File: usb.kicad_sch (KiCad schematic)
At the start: 26 parts, among them J1 USB_A, J2 USB_A, J4 USB_C_Receptacle_USB2.0, U1 FE1.1s, U3 SRV05-4, U4 SRV05-4, U6 AP2552W6, Y1 12MHz

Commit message: routing progress
Just nice to make some save points every now and again.
USB seems... ok?  Still need to check 3v3 or 5v on the power pullups,
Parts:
- removed U3: SRV05-4, Package_TO_SOT_SMD:SOT-23-6, symbol Power_Protection:SRV05-4
- added U3: SRV05-4, Package_TO_SOT_SMD:SOT-23-6, symbol karl-parts:SRV05-4
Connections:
- net GND: now also U3.2 (GND)
- net UDS1N: now also U1.10 (DM1), U3.6 (I/O4); no longer U1.8 (DM2)
- net UDS1P: now also U1.11 (DP1), U3.1 (I/O1); no longer U1.9 (DP2)
- net UDS2N: now also U1.8 (DM2), U3.4 (I/O3); no longer U1.6 (DM3)
- net UDS2P: now also U1.9 (DP2), U3.3 (I/O2); no longer U1.7 (DP3)
- net UMCU_N: now also U1.6 (DM3); no longer U1.10 (DM1)
- net UMCU_P: now also U1.7 (DP3); no longer U1.11 (DP1)
- net UUPN: now also U4.3 (IO2); no longer U4.1 (IO1)
- net UUPP: now also U4.4 (IO3); no longer U4.3 (IO2)
- net VBUS: now also U3.5 (VBUS)
- no-connect marks 9 -> 11
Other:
- note added: "Do these need to be 3v3?! these are from the switch?"
- note added: "TODO - ground?"
- moved on the sheet: U4

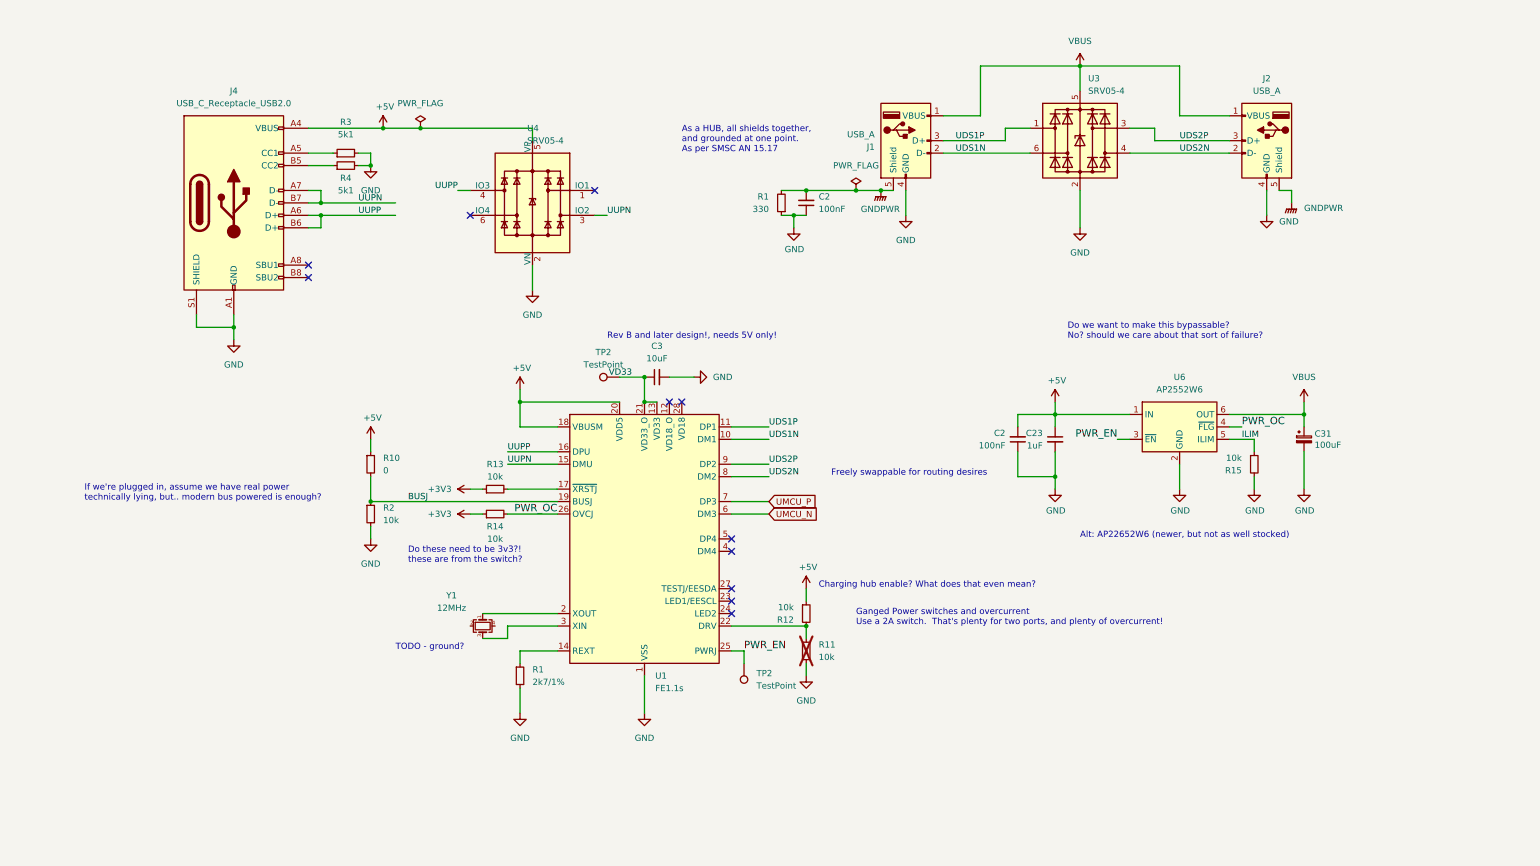
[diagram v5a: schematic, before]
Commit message: cleanup schematic, break out most of it
Broke it all out to the right places, now I can go and shuffle all the
labels to make it line up.  Thankfully we can just "freely" route the
keybaord matrix pins!
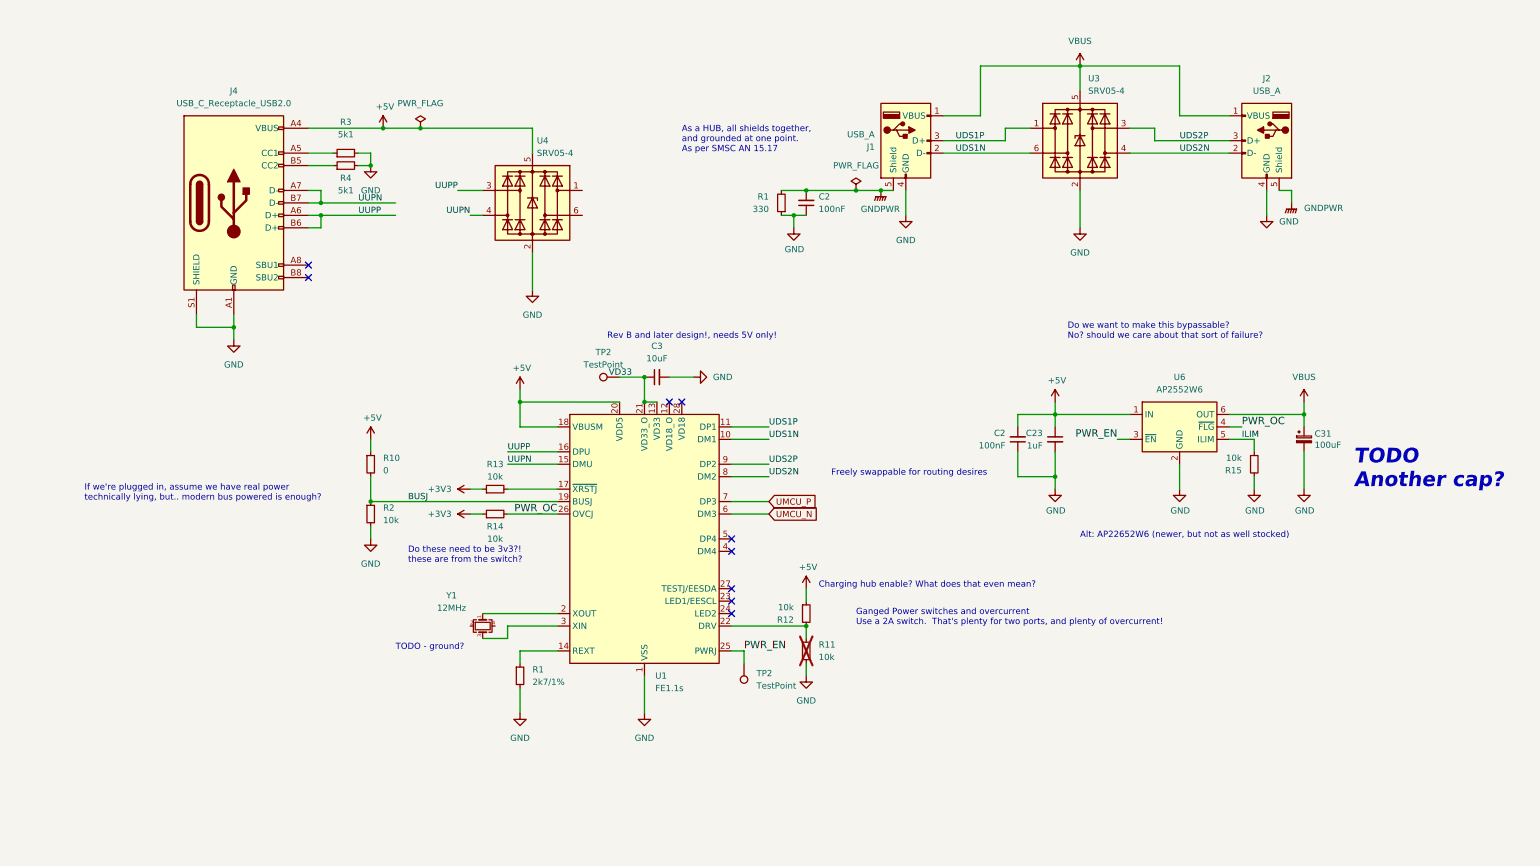
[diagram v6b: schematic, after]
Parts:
- U4: symbol Power_Protection:SRV05-4 -> karl-parts:SRV05-4
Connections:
- net UUPN: now also U4.4 (I/O3); no longer U4.3 (IO2)
- net UUPP: now also U4.3 (I/O2); no longer U4.4 (IO3)
- no-connect marks 11 -> 9
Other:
- note added: "TODO Another cap?"
- company: (none) -> Ekta Labs
- title: (none) -> Das KB4-Bara2
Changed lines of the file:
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@@
 (kicad_sch (version 20230121) (generator eeschema)
   (paper "A4")
+  (title_block
+    (title "Das KB4-Bara2")
+    (company "Ekta Labs")
+    (comment 1 "http://github.com/karlp/das-kb4-bara2")
+  )
   (junction (at 86.36 45.72) (diameter 0) (color 0 0 0 0)
   )
@@
   (no_connect (at 160.02 121.92))
   (no_connect (at 147.32 93.98))
-  (no_connect (at 132.08 50.8))
   (no_connect (at 160.02 124.46))
   (no_connect (at 160.02 137.16))
   (no_connect (at 73.66 68.58))
-  (no_connect (at 106.68 55.88))
   (no_connect (at 160.02 132.08))
   (no_connect (at 149.86 93.98))
@@
     (stroke (width 0) (type default))
   )
+  (wire (pts (xy 106.68 55.88) (xy 109.22 55.88))
+    (stroke (width 0) (type default))
+  )
   (wire (pts (xy 86.36 114.3) (xy 124.46 114.3))
     (stroke (width 0) (type default))
@@
     (stroke (width 0) (type default))
   )
-  (wire (pts (xy 132.08 55.88) (xy 134.62 55.88))
-    (stroke (width 0) (type default))
-  )
   (wire (pts (xy 114.3 139.7) (xy 114.3 142.24))
     (stroke (width 0) (type default))
@@
     (stroke (width 0) (type default))
   )
-  (wire (pts (xy 119.38 66.04) (xy 119.38 71.12))
+  (wire (pts (xy 119.38 63.5) (xy 119.38 71.12))
     (stroke (width 0) (type default))
   )
@@
     (stroke (width 0) (type default))
   )
-  (wire (pts (xy 119.38 40.64) (xy 119.38 38.1))
-    (stroke (width 0) (type default))
-  )
   (wire (pts (xy 218.44 109.22) (xy 226.06 109.22))
     (stroke (width 0) (type default))
@@
     (stroke (width 0) (type default))
   )
+  (wire (pts (xy 119.38 38.1) (xy 119.38 43.18))
+    (stroke (width 0) (type default))
+  )
   (wire (pts (xy 114.3 106.68) (xy 124.46 106.68))
     (stroke (width 0) (type default))
@@
     (stroke (width 0) (type default))
   )
-  (wire (pts (xy 104.14 50.8) (xy 106.68 50.8))
+  (wire (pts (xy 104.14 50.8) (xy 109.22 50.8))
     (stroke (width 0) (type default))
   )
@@
     (effects (font (size 1.27 1.27)) (justify left bottom))
   )
+  (text "TODO\nAnother cap?" (at 287.02 111.76 0)
+    (effects (font (size 3 3) (thickness 0.6) bold italic (color 255 16 105 1)) (justify left bottom))
+  )
   (text "Rev B and later design!, needs 5V only!" (at 134.62 81.28 0)
     (effects (font (size 1.27 1.27)) (justify left bottom))
@@
     (effects (font (size 1.27 1.27)) (justify left bottom))
   )
-  (label "UUPN" (at 134.62 55.88 0) (fields_autoplaced)
-    (effects (font (size 1.27 1.27)) (justify left bottom))
-  )
   (label "UUPN" (at 83.82 53.34 0) (fields_autoplaced)
     (effects (font (size 1.27 1.27)) (justify left bottom))
@@
   (label "UDS2N" (at 251.46 43.18 0) (fields_autoplaced)
     (effects (font (size 1.27 1.27)) (justify left bottom))
+  )
+  (label "UUPN" (at 106.68 55.88 180) (fields_autoplaced)
+    (effects (font (size 1.27 1.27)) (justify right bottom))
   )
   (label "UDS1N" (at 205.74 43.18 0) (fields_autoplaced)
@@
     )
   )
-  (symbol (lib_id "Power_Protection:SRV05-4") (at 119.38 53.34 0) (mirror y) (unit 1)
+  (symbol (lib_id "karl-parts:SRV05-4") (at 119.38 53.34 0) (mirror y) (unit 1)
     (in_bom yes) (on_board yes) (dnp no) (fields_autoplaced)
-    (property "Reference" "U4" (at 118.2939 38.1 0)
+    (property "Reference" "U4" (at 120.2689 40.64 0)
       (effects (font (size 1.27 1.27)) (justify right))
     )
-    (property "Value" "SRV05-4" (at 118.2939 40.64 0)
+    (property "Value" "SRV05-4" (at 120.2689 43.18 0)
       (effects (font (size 1.27 1.27)) (justify right))
     )
-    (property "Footprint" "Package_TO_SOT_SMD:SOT-23-6" (at 101.6 64.77 0)
-      (effects (font (size 1.27 1.27)) hide)
-    )
-    (property "Datasheet" "http://www.onsemi.com/pub/Collateral/SRV05-4-D.PDF" (at 119.38 53.34 0)
-      (effects (font (size 1.27 1.27)) hide)
-    )
+    (property "Footprint" "Package_TO_SOT_SMD:SOT-23-6" (at 119.38 66.04 0)
+      (effects (font (size 1.27 1.27)) hide)
+    )
+    (property "Datasheet" "http://www.onsemi.com/pub/Collateral/SRV05-4-D.PDF" (at 114.3 44.45 0)
+      (effects (font (size 1.27 1.27)) hide)
+    )

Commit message: unrouted: 0
Juggled all the key matrix IOs and reviewed "all" outstanding TODOs

left: add another cap for downstream Vbus.  it's free, and can only
help.

left: lots of silk?
left: place as much free io to pads as can be easily done, for
test/board reuse.
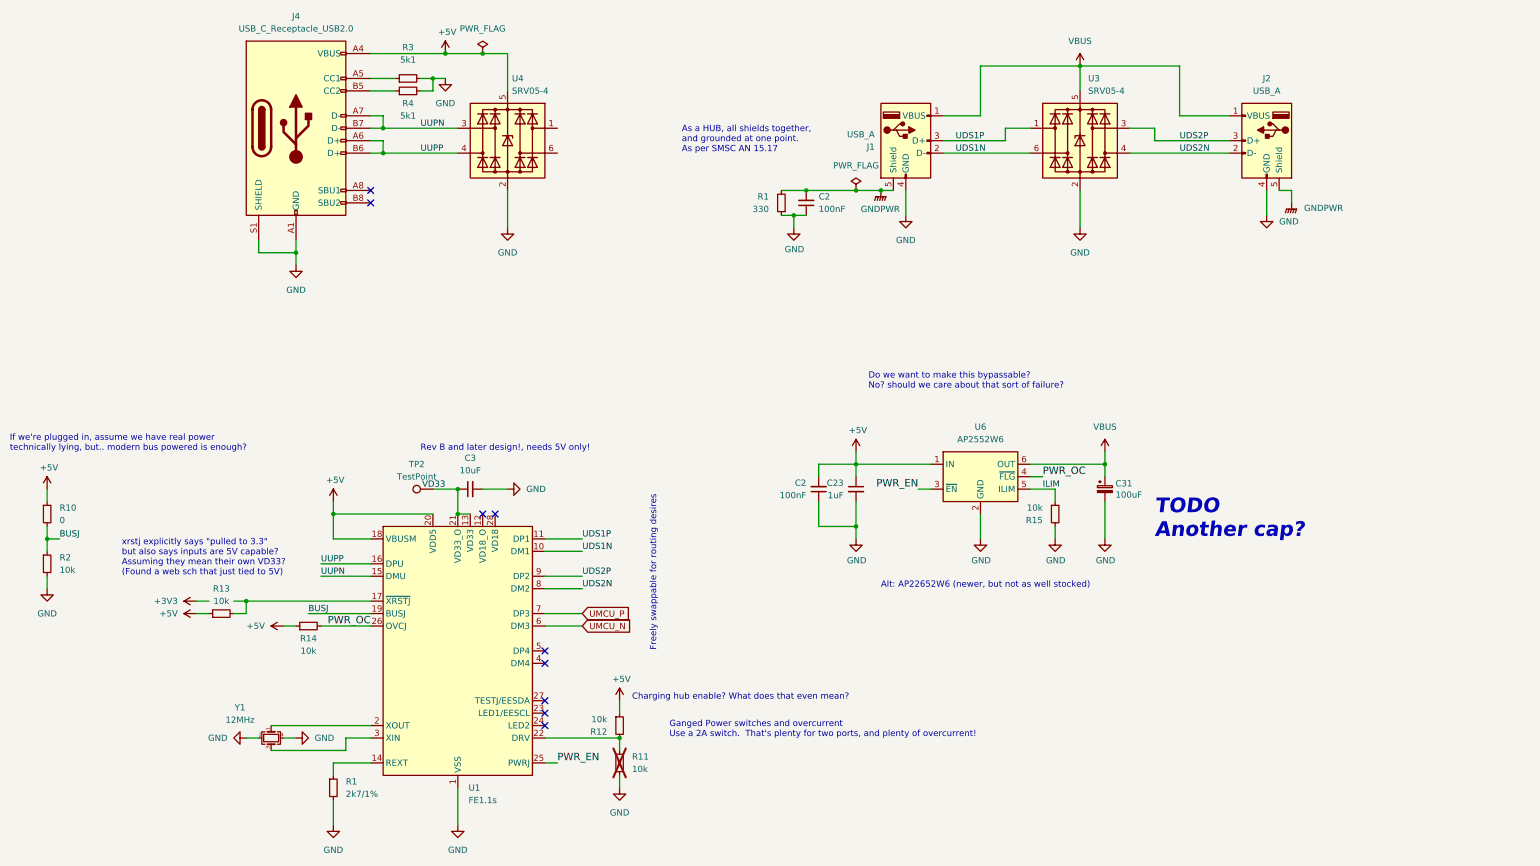
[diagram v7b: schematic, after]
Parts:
- removed TP2: TestPoint, TestPoint:TestPoint_THTPad_D1.5mm_Drill0.7mm, symbol Connector:TestPoint
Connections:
- net +3V3: no longer R13.1, R14.1
- net +5V: now also R13.1, R14.1
- net GND: now also Y1.2, Y1.4
- net UUPN: now also U4.3 (I/O2); no longer U4.4 (I/O3)
- net UUPP: now also U4.4 (I/O3); no longer U4.3 (I/O2)
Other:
- note added: "xrstj explicitly says "pulled to 3.3" but also says inputs are 5V capable? Assuming they mean their own VD33? (Found a web sch that just tied to 5V)"
- note removed: "Do these need to be 3v3?! these are from the switch?"
- note removed: "TODO - ground?"
- moved on the sheet: C2, C23, C3, C31, J4, R1, R10, R11, R12, R13, R14, R15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

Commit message: shuffled, added bonus, silked up...
Nearly there..?
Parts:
- added C31: 100uF, Capacitor_SMD:C_1206_3216Metric, symbol Device:C_Polarized_Small
- R1: value 330 -> 220; MPN 0603WAF3300T5E -> 0603WAF2200T5E; lcsc# C23138 -> C22962
- TP2: value TestPoint -> VD33
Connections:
- net GND: now also C31.2
- net VBUS: now also C31.1
- no-connect marks 9 -> 11
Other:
- note added: "Charging hub enable? What does that even mean? (allegedly, means can give dumb DS devs >= 500mA?)"
- note removed: "Charging hub enable? What does that even mean?"
- note removed: "Do we want to make this bypassable? No? should we care about that sort of failure?"
- note removed: "TODO Another cap?"
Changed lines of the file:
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@@
   (junction (at 172.72 55.88) (diameter 0) (color 0 0 0 0)
+  )
+  (junction (at 236.22 119.38) (diameter 0) (color 0 0 0 0)
   )
   (junction (at 104.14 111.76) (diameter 0) (color 0 0 0 0)
@@
   (no_connect (at 121.92 147.32))
   (no_connect (at 121.92 160.02))
+  (no_connect (at 124.46 43.18))
   (no_connect (at 86.36 53.34))
+  (no_connect (at 124.46 38.1))
   (no_connect (at 121.92 154.94))
   (no_connect (at 111.76 116.84))
@@
     (stroke (width 0) (type default))
   )
+  (wire (pts (xy 246.38 106.68) (xy 236.22 106.68))
+    (stroke (width 0) (type default))
+  )
   (wire (pts (xy 121.92 139.7) (xy 129.54 139.7))
     (stroke (width 0) (type default))
@@
     (stroke (width 0) (type default))
   )
+  (wire (pts (xy 246.38 109.22) (xy 246.38 106.68))
+    (stroke (width 0) (type default))
+  )
   (wire (pts (xy 78.74 114.3) (xy 78.74 116.84))
     (stroke (width 0) (type default))
@@
     (stroke (width 0) (type default))
   )
+  (wire (pts (xy 246.38 119.38) (xy 236.22 119.38))
+    (stroke (width 0) (type default))
+  )
   (wire (pts (xy 190.5 50.8) (xy 193.04 50.8))
     (stroke (width 0) (type solid))
@@
     (stroke (width 0) (type default))
   )
-  (wire (pts (xy 236.22 114.3) (xy 236.22 121.92))
+  (wire (pts (xy 236.22 114.3) (xy 236.22 119.38))
     (stroke (width 0) (type solid))
   )
@@
     (stroke (width 0) (type default))
   )
+  (wire (pts (xy 246.38 114.3) (xy 246.38 119.38))
+    (stroke (width 0) (type default))
+  )
   (wire (pts (xy 63.5 63.5) (xy 71.12 63.5))
     (stroke (width 0) (type default))
@@
     (stroke (width 0) (type default))
   )
+  (wire (pts (xy 236.22 119.38) (xy 236.22 121.92))
+    (stroke (width 0) (type solid))
+  )
   (wire (pts (xy 99.06 27.94) (xy 96.52 27.94))
     (stroke (width 0) (type default))
@@
     (effects (font (size 1.27 1.27)) (justify left bottom))
   )
-  (text "Do we want to make this bypassable?\nNo? should we care about that sort of failure?"
-    (at 187.96 91.44 0)
-    (effects (font (size 1.27 1.27)) (justify left bottom))
-  )
   (text "If we're plugged in, assume we have real power\ntechnically lying, but.. modern bus powered is enough?"
     (at 12.7 104.14 0)
     (effects (font (size 1.27 1.27)) (justify left bottom))
   )
-  (text "TODO\nAnother cap?" (at 246.38 121.92 0)
-    (effects (font (size 3 3) (thickness 0.6) bold italic (color 255 16 105 1)) (justify left bottom))
-  )
   (text "Rev B and later design!, needs 5V only!" (at 96.52 104.14 0)
     (effects (font (size 1.27 1.27)) (justify left bottom))
   )
-  (text "Charging hub enable? What does that even mean?" (at 139.7 154.94 0)
+  (text "Charging hub enable? What does that even mean?\n(allegedly, means can give dumb DS devs >= 500mA?)"
+    (at 139.7 154.94 0)
     (effects (font (size 1.27 1.27)) (justify left bottom))
   )
@@
       (effects (font (size 1.27 1.27)) (justify left))
     )
-    (property "Value" "330" (at 167.64 54.61 0)
+    (property "Value" "220" (at 167.64 54.61 0)
       (effects (font (size 1.27 1.27)) (justify left))
     )
@@
       (effects (font (size 1.27 1.27)) hide)
     )
-    (property "MPN" "0603WAF3300T5E" (at 170.18 53.34 0)
+    (property "MPN" "0603WAF2200T5E" (at 170.18 53.34 0)
       (effects (font (size 1.27 1.27)) hide)
     )
@@
       (effects (font (size 1.27 1.27)) hide)
     )
-    (property "lcsc#" "C23138" (at 170.18 53.34 0)
+    (property "lcsc#" "C22962" (at 170.18 53.34 0)
       (effects (font (size 1.27 1.27)) hide)
     )
@@
       (effects (font (size 1.27 1.27)))
     )
-    (property "Value" "TestPoint" (at 95.758 109.22 90)
+    (property "Value" "VD33" (at 95.758 109.22 90)
       (effects (font (size 1.27 1.27)))
     )
@@
         )
       )
+    )
+  )
+  (symbol (lib_id "Device:C_Polarized_Small") (at 246.38 111.76 0) (unit 1)
+    (in_bom yes) (on_board yes) (dnp no)
+    (property "Reference" "C31" (at 248.5391 110.6106 0)
+      (effects (font (size 1.27 1.27)) (justify left))
+    )
+    (property "Value" "100uF" (at 248.539 112.909 0)
+      (effects (font (size 1.27 1.27)) (justify left))
+    )
+    (property "Footprint" "Capacitor_SMD:C_1206_3216Metric" (at 246.38 111.76 0)
+      (effects (font (size 1.27 1.27)) hide)
+    )
+    (property "Datasheet" "~" (at 246.38 111.76 0)
+      (effects (font (size 1.27 1.27)) hide)
+    )
+    (property "MPN" "CL31A107MQHNNNE" (at 246.38 111.76 0)
+      (effects (font (size 1.27 1.27)) hide)
+    )
+    (property "jlc-basic" "1" (at 246.38 111.76 0)
+      (effects (font (size 1.27 1.27)) hide)
+    )
+    (property "lcsc#" "C15008" (at 246.38 111.76 0)
+      (effects (font (size 1.27 1.27)) hide)
+    )
+    (property "lcsc2#" "" (at 246.38 111.76 0)
+      (effects (font (size 1.27 1.27)) hide)
+    )
+    (pin "1")
+    (pin "2")
+    (instances
+      (project "r2022-12"
+        (path "/9d3292e9-89ed-435a-b615-fc52a41b2a3d/00000000-0000-0000-0000-00005e1ad41f"
+          (reference "C31") (unit 1)
+        )
+      )
+      (project "das-kb4-bara2"
+        (path "/d0e4eaec-96cb-4a0e-a384-5b3e3f5f8d5d/f457a5c4-270e-459d-a4f0-150cf90e3909"
+          (reference "C16") (unit 1)
+        )
+      )
